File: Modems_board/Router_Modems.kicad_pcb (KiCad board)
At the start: 2 copper layers, 87 parts, among them U1 SRV05-4, U2 TPS54540, U3 SRV05-4, U4 TPS54540, U5 SRV05-4, U6 SRV05-4, X1 SIM_Card, X10 SIM_Card, X11 Bus_M.2_Socket_B, X12 S4B-XH, X13 S4B-XH, X2 B2B-XH, X3 Bus_M.2_Socket_B, X4 SIM_Card, X5 Bus_M.2_Socket_B, X6 SIM_Card, X7 Bus_M.2_Socket_B, X8 S4B-XH, X9 S4B-XH

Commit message: routing procs
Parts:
- removed H6: M3, MountingHole:MountingHole_3.5mm_Pad
- C10, C12, C13, C14, C15, C16, C17, C18, C19, C2, C20, C21, C22, C24, C25, C26, C27, C28, C29, C3, C31, C32, C33, C34, C4, C5, C6, C7, C8, C9, D2, D4, N1, N2, N3, N4, R1, R10, R11, R12, R13, R14, R15, R16, R2, R3, R4, R5, R6, R7, R8, R9, U2, U4, X11, X3, X5, X7: moved to B.Cu
- X12, X13, X8, X9: footprint Connector_JST:JST_XH_S4B-XH-A_1x04_P2.50mm_Horizontal -> Connector_JST:JST_XH_B4B-XH-A_1x04_P2.50mm_Vertical
- moved N4 208.4 mm to (64.0, 130.2), turned to 90 degrees
- moved N1 199.4 mm to (63.9, 54.1), turned to 90 degrees
- moved H3 194.2 mm to (60.2, 178.3)
- moved R6 192.0 mm to (78.0, 113.8)
- moved H1 188.3 mm to (60.2, 38.3)
- moved C19 184.6 mm to (92.0, 111.9), turned to -90 degrees
- moved C32 183.1 mm to (99.0, 38.0), turned to 180 degrees
- moved C9 182.8 mm to (75.8, 112.3)
- moved H5 179.5 mm to (105.2, 178.3)
- moved R10 178.5 mm to (102.2, 105.7)
- moved L1 177.1 mm to (71.5, 107.6), turned to 180 degrees
- moved C22 173.3 mm to (98.9, 113.8)
- moved X3 165.3 mm to (104.2, 130.2), turned to 90 degrees
- moved C11 165.2 mm to (100.9, 161.6), turned to 90 degrees
- moved C7 164.2 mm to (103.4, 115.8)
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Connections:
- U1 pad 1: /SIM1_DAT -> /SIM1_CLK
- U1 pad 3: /SIM1_CLK -> unconnected-(U1-Pad3)
- U1 pad 4: /SIM1_RST -> /SIM1_DAT
- U1 pad 6: unconnected-(U1-Pad6) -> /SIM1_RST
- U3 pad 1: /SIM2_DAT -> /SIM2_CLK
- U3 pad 3: /SIM2_CLK -> unconnected-(U3-Pad3)
- U3 pad 4: /SIM2_RST -> /SIM2_DAT
- U3 pad 6: unconnected-(U3-Pad6) -> /SIM2_RST
- U5 pad 1: /SIM3_DAT -> /SIM3_CLK
- U5 pad 3: /SIM3_CLK -> unconnected-(U5-Pad3)
- U5 pad 4: /SIM3_RST -> /SIM3_DAT
- U5 pad 6: unconnected-(U5-Pad6) -> /SIM3_RST
- U6 pad 1: /SIM4_DAT -> /SIM4_CLK
- U6 pad 3: /SIM4_CLK -> unconnected-(U6-Pad3)
- U6 pad 4: /SIM4_RST -> /SIM4_DAT
- U6 pad 6: unconnected-(U6-Pad6) -> /SIM4_RST
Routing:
- net /SIM1_DAT: track 0.00 -> 36.6 mm, vias 0 -> 1
- net /SIM2_DAT: track 0.00 -> 36.6 mm, vias 0 -> 1
- net /SIM3_DAT: track 0.00 -> 36.3 mm, vias 0 -> 1
- net /SIM4_DAT: track 0.00 -> 36.3 mm, vias 0 -> 1
- net /SIM1_CLK: track 0.00 -> 21.3 mm, vias 0 -> 1
- net /SIM4_CLK: track 0.00 -> 21.2 mm, vias 0 -> 1
- net /SIM2_CLK: track 0.00 -> 21.2 mm, vias 0 -> 1
- net /SIM3_CLK: track 0.00 -> 21.1 mm, vias 0 -> 1
- net /M3_ONOFF: track 0.00 -> 18.1 mm
- net /M2_ONOFF: track 0.00 -> 18.1 mm
- net /M4_ONOFF: track 0.00 -> 18.1 mm
- net /M1_ONOFF: track 0.00 -> 17.9 mm
- net Net-(R14-Pad1): track 0.00 -> 15.7 mm
- net Net-(R16-Pad1): track 0.00 -> 15.6 mm
- net Net-(R8-Pad1): track 0.00 -> 15.6 mm
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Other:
- board outline added: 62 x 148 mm

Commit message: Modems board ready
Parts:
- added C35: 100u, Capacitor_Tantalum_SMD:CP_EIA-3528-15_AVX-H, B.Cu at (67.1, 103.7)
- added C36: 100u, Capacitor_Tantalum_SMD:CP_EIA-3528-15_AVX-H, B.Cu at (114.7, 112.3)
- added C37: 100u 50V, Capacitor_SMD:CP_Elec_10x10.5, F.Cu at (90.5, 107.6)
- X12, X13, X8, X9: value S4B-XH -> B4B-XH
- moved C7 4.75 mm to (108.2, 115.9)
- moved C5 4.70 mm to (107.4, 117.9)
- moved C12 1.98 mm to (68.3, 112.1)
- moved C14 1.97 mm to (71.8, 112.1)
- moved C24 1.95 mm to (112.8, 104.4)
- moved C26 1.92 mm to (109.3, 104.4)
- moved C20 0.84 mm to (106.1, 105.8)
- moved R10 0.84 mm to (103.0, 105.8)
- moved C9 0.84 mm to (76.6, 112.2)
- moved C21 0.83 mm to (104.5, 104.2)
- moved R6 0.83 mm to (78.8, 113.8)
- moved C18 0.83 mm to (90.4, 111.9)
- moved C19 0.83 mm to (92.8, 111.9)
- moved C22 0.83 mm to (99.8, 113.8)
- moved C4 0.83 mm to (90.4, 104.2)
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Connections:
- C12 pad 1: +3V3A -> +3V3B
- C14 pad 1: +3V3A -> +3V3B
- L1 pad 2: +3V3A -> +3V3B
- R6 pad 1: +3V3A -> +3V3B
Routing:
- net GND: track 0.00 -> 116.6 mm, vias 0 -> 182
- net +3V3A: track 5.18 -> 71.6 mm, vias 0 -> 13
- net +3V3B: track 5.36 -> 71.2 mm, vias 0 -> 14
- net VCC: track 0.00 -> 31.5 mm, vias 0 -> 12
- net Net-(C10-Pad1): track 0.00 -> 10.6 mm, vias 0 -> 2
- net Net-(C22-Pad1): track 0.00 -> 10.6 mm, vias 0 -> 2
- net Net-(C21-Pad2): track 0.00 -> 4.42 mm
- net Net-(C9-Pad2): track 0.00 -> 4.01 mm
- net Net-(R6-Pad2): track 0.00 -> 3.50 mm
- net Net-(R12-Pad2): track 0.00 -> 3.45 mm
- net Net-(C22-Pad2): track 0.00 -> 3.02 mm, vias 0 -> 9
- net Net-(C10-Pad2): track 0.00 -> 3.00 mm, vias 0 -> 9
- net Net-(R2-Pad1): track 0.00 -> 2.10 mm
- net Net-(R9-Pad1): track 0.00 -> 2.07 mm
- net Net-(C20-Pad1): track 0.00 -> 1.45 mm
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- added copper zone on B.Cu, net +3V3A
- added copper zone on B.Cu, net +3V3B
- added copper zone on B.Cu, net GND
- added copper zone on F.Cu, net GND
- added copper zone on B.Cu, net Net-(C10-Pad2)
- added copper zone on B.Cu, net Net-(C22-Pad2)
- added copper zone on B.Cu, net VCC
- added copper zone on F.Cu, net VCC
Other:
- board text added: "LOCK"
- board text added: "OPEN"

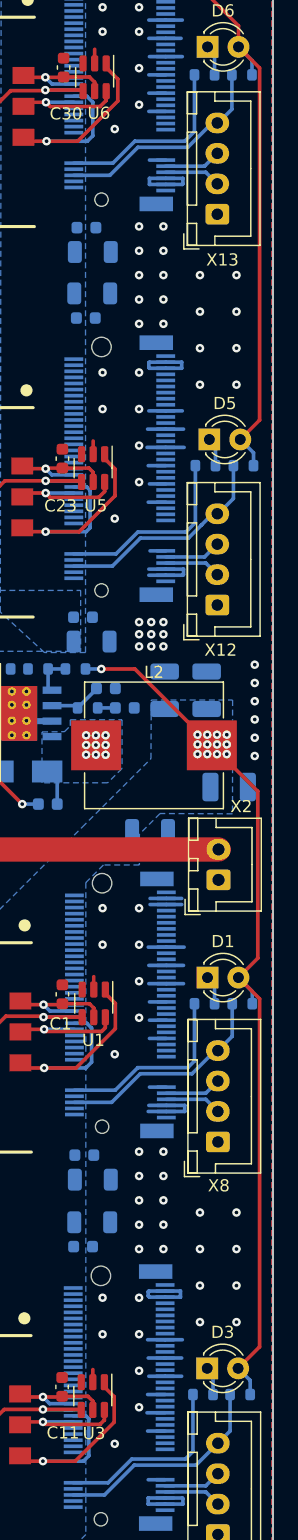
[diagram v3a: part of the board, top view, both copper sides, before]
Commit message: remove modems gpio ctrls
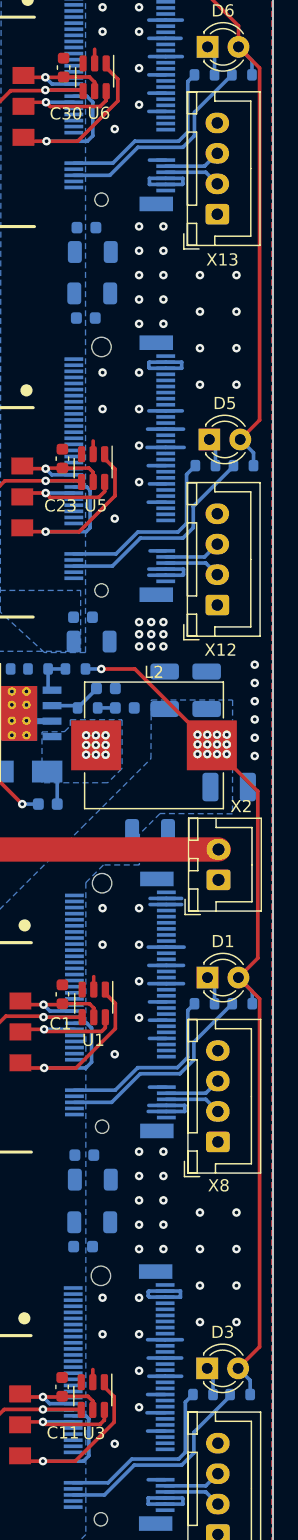
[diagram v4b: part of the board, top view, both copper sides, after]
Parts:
- R10, R4: value 47k -> 43k
- R14, R16, R3, R8: value 470 -> 470R
- X11, X3, X5, X7: value Bus_M.2_Socket_B -> AS0BC21-S30BB-7H
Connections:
- X12 pad 4: /M3_ONOFF -> GND
- X13 pad 4: /M4_ONOFF -> GND
- X8 pad 4: /M1_ONOFF -> GND
- X9 pad 4: /M2_ONOFF -> GND
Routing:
- net /M1_ONOFF: track 17.9 -> 17.2 mm
- net /M2_ONOFF: track 18.1 -> 17.4 mm
- net /M3_ONOFF: track 18.1 -> 17.6 mm
- net /M4_ONOFF: track 18.1 -> 17.5 mm
